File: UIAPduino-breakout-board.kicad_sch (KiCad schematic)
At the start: 5 parts, among them J1 Conn_01x20_Pin, J2 Conn_01x20_Socket

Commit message: FP 割り当て
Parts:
- J1: footprint (none) -> Connector_PinHeader_2.54mm:PinHeader_1x20_P2.54mm_Vertical
- J2: footprint (none) -> Connector_PinSocket_2.54mm:PinSocket_1x20_P2.54mm_Vertical
- JP1: footprint (none) -> Jumper:SolderJumper-2_P1.3mm_Open_TrianglePad1.0x1.5mm
- U1: footprint (none) -> akizuki:FT234X
- U2: footprint (none) -> UIAP-Devices:UIAPDUINO-PRO-MICRO-CH32V003-V1DOT4
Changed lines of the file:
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@@
 			)
 		)
-		(property "Footprint" ""
+		(property "Footprint" "Jumper:SolderJumper-2_P1.3mm_Open_TrianglePad1.0x1.5mm"
 			(at 152.4 52.07 0)
 			(effects
@@
 			)
 		)
-		(property "Footprint" ""
+		(property "Footprint" "Connector_PinHeader_2.54mm:PinHeader_1x20_P2.54mm_Vertical"
 			(at 210.82 45.72 0)
 			(effects
@@
 			)
 		)
-		(property "Footprint" ""
+		(property "Footprint" "Connector_PinSocket_2.54mm:PinSocket_1x20_P2.54mm_Vertical"
 			(at 210.82 132.08 0)
 			(effects
@@
 			)
 		)
-		(property "Footprint" ""
+		(property "Footprint" "akizuki:FT234X"
 			(at 111.76 38.1 0)
 			(effects
@@
 			)
 		)
-		(property "Footprint" ""
+		(property "Footprint" "UIAP-Devices:UIAPDUINO-PRO-MICRO-CH32V003-V1DOT4"
 			(at 152.4 58.42 0)
 			(effects

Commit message: 回路修正
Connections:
- net GND: no longer J1.7 (Pin_7), J2.7 (Pin_7)
- net at J1.8 (Pin_8), J2.8 (Pin_8): now also U2.18 (0/A1); no longer U2.22 (~{RESET})
- net at J1.9 (Pin_9), J2.9 (Pin_9), U2.17 (1/A0): no longer U2.18 (0/A1)
- new net: J1.7 (Pin_7), J2.7 (Pin_7), U2.22 (~{RESET})
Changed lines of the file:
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@@
 	(paper "A4")
 	(junction
-		(at 208.28 76.2)
-		(diameter 0)
-		(color 0 0 0 0)
-	)
-	(junction
 		(at 208.28 78.74)
 		(diameter 0)
@@
 	)
 	(junction
-		(at 205.74 66.04)
-		(diameter 0)
-		(color 0 0 0 0)
-	)
-	(junction
 		(at 223.52 81.28)
 		(diameter 0)
@@
 	)
 	(junction
+		(at 205.74 76.2)
+		(diameter 0)
+		(color 0 0 0 0)
+	)
+	(junction
 		(at 220.98 73.66)
 		(diameter 0)
@@
 	)
 	(junction
-		(at 203.2 58.42)
+		(at 203.2 66.04)
 		(diameter 0)
 		(color 0 0 0 0)
@@
 	(wire
 		(pts
-			(xy 208.28 78.74) (xy 208.28 76.2)
-		)
-		(stroke
-			(width 0)
-			(type default)
-		)
-	)
-	(wire
-		(pts
 			(xy 220.98 50.8) (xy 220.98 73.66)
 		)
@@
 	(wire
 		(pts
+			(xy 200.66 58.42) (xy 243.84 58.42)
+		)
+		(stroke
+			(width 0)
+			(type default)
+		)
+	)
+	(wire
+		(pts
 			(xy 132.08 76.2) (xy 134.62 76.2)
 		)
@@
 	(wire
 		(pts
+			(xy 203.2 66.04) (xy 203.2 127)
+		)
+		(stroke
+			(width 0)
+			(type default)
+		)
+	)
+	(wire
+		(pts
 			(xy 233.68 119.38) (xy 233.68 50.8)
 		)
@@
 	(wire
 		(pts
-			(xy 205.74 127) (xy 205.74 66.04)
+			(xy 205.74 50.8) (xy 205.74 76.2)
 		)
 		(stroke
@@
 	(wire
 		(pts
-			(xy 200.66 58.42) (xy 203.2 58.42)
-		)
-		(stroke
-			(width 0)
-			(type default)
-		)
-	)
-	(wire
-		(pts
 			(xy 170.18 60.96) (xy 172.72 60.96)
 		)
@@
 	(wire
 		(pts
-			(xy 208.28 76.2) (xy 208.28 50.8)
+			(xy 208.28 50.8) (xy 208.28 78.74)
 		)
 		(stroke
@@
 	(wire
 		(pts
-			(xy 203.2 58.42) (xy 203.2 127)
+			(xy 203.2 50.8) (xy 203.2 66.04)
 		)
 		(stroke
@@
 	(wire
 		(pts
-			(xy 203.2 50.8) (xy 203.2 58.42)
-		)
-		(stroke
-			(width 0)
-			(type default)
-		)
-	)
-	(wire
-		(pts
 			(xy 200.66 58.42) (xy 200.66 127)
 		)
@@
 	(wire
 		(pts
-			(xy 170.18 76.2) (xy 208.28 76.2)
+			(xy 170.18 76.2) (xy 205.74 76.2)
 		)
 		(stroke
@@
 	(wire
 		(pts
-			(xy 205.74 66.04) (xy 205.74 50.8)
-		)
-		(stroke
-			(width 0)
-			(type default)
-		)
-	)
-	(wire
-		(pts
 			(xy 172.72 52.07) (xy 172.72 60.96)
 		)
@@
 	(wire
 		(pts
+			(xy 205.74 76.2) (xy 205.74 127)
+		)
+		(stroke
+			(width 0)
+			(type default)
+		)
+	)
+	(wire
+		(pts
 			(xy 195.58 55.88) (xy 195.58 127)
 		)
@@
 	(wire
 		(pts
-			(xy 203.2 58.42) (xy 243.84 58.42)
-		)
-		(stroke
-			(width 0)
-			(type default)
-		)
-	)
-	(wire
-		(pts
-			(xy 170.18 66.04) (xy 205.74 66.04)
-		)
-		(stroke
+			(xy 170.18 66.04) (xy 203.2 66.04)
+		)
+		(stroke

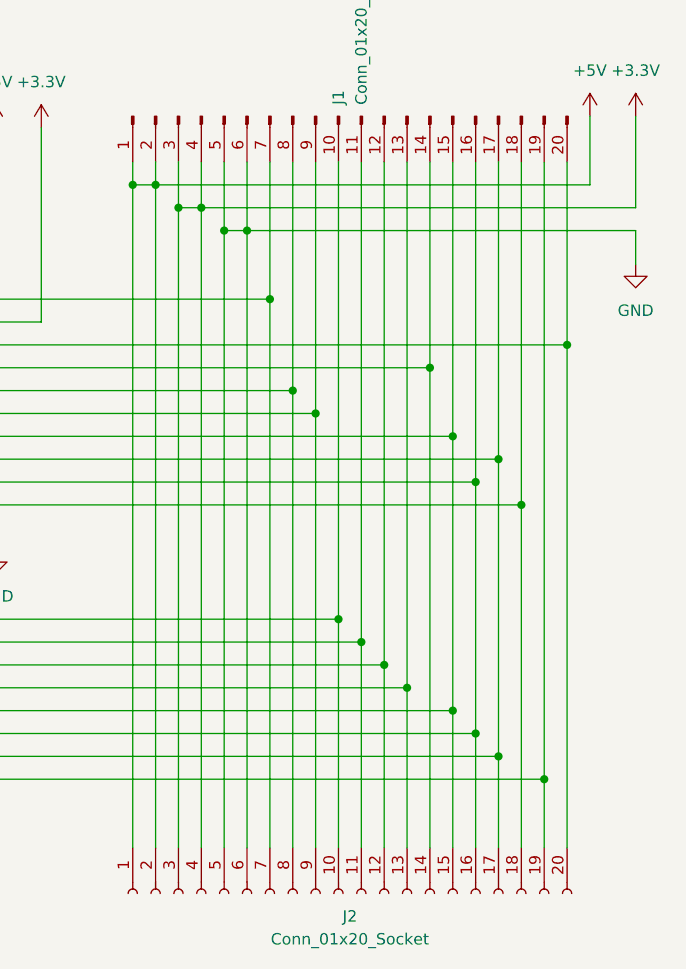
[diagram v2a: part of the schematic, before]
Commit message: 電源配置を変更
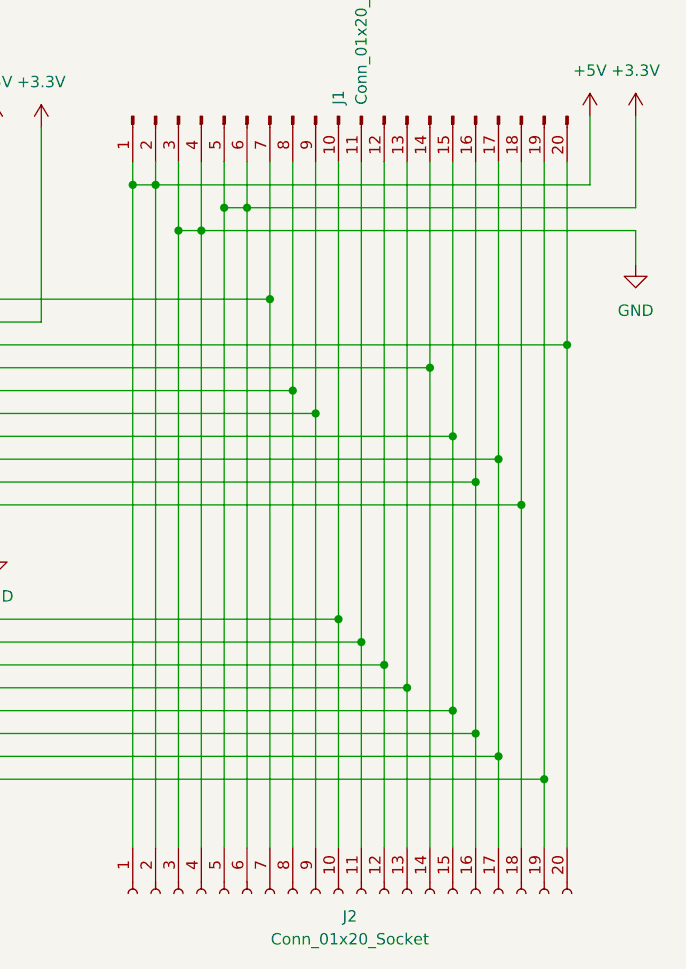
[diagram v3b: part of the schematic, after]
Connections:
- net +3.3V: now also J1.5 (Pin_5), J1.6 (Pin_6), J2.5 (Pin_5), J2.6 (Pin_6); no longer J1.3 (Pin_3), J1.4 (Pin_4), J2.3 (Pin_3), J2.4 (Pin_4)
- net GND: now also J1.3 (Pin_3), J1.4 (Pin_4), J2.3 (Pin_3), J2.4 (Pin_4); no longer J1.5 (Pin_5), J1.6 (Pin_6), J2.5 (Pin_5), J2.6 (Pin_6)
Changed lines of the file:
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@@
 	(paper "A4")
 	(junction
+		(at 195.58 58.42)
+		(diameter 0)
+		(color 0 0 0 0)
+	)
+	(junction
 		(at 208.28 78.74)
 		(diameter 0)
@@
 	)
 	(junction
+		(at 200.66 55.88)
+		(diameter 0)
+		(color 0 0 0 0)
+	)
+	(junction
 		(at 223.52 81.28)
 		(diameter 0)
@@
 	)
 	(junction
+		(at 193.04 58.42)
+		(diameter 0)
+		(color 0 0 0 0)
+	)
+	(junction
 		(at 210.82 101.6)
 		(diameter 0)
@@
 	)
 	(junction
-		(at 198.12 58.42)
-		(diameter 0)
-		(color 0 0 0 0)
-	)
-	(junction
 		(at 228.6 116.84)
 		(diameter 0)
@@
 	)
 	(junction
-		(at 195.58 55.88)
-		(diameter 0)
-		(color 0 0 0 0)
-	)
-	(junction
 		(at 190.5 53.34)
 		(diameter 0)
@@
 	)
 	(junction
-		(at 193.04 55.88)
-		(diameter 0)
-		(color 0 0 0 0)
-	)
-	(junction
 		(at 226.06 114.3)
 		(diameter 0)
@@
 	)
 	(junction
+		(at 198.12 55.88)
+		(diameter 0)
+		(color 0 0 0 0)
+	)
+	(junction
 		(at 205.74 76.2)
 		(diameter 0)
@@
 	)
 	(junction
-		(at 200.66 58.42)
-		(diameter 0)
-		(color 0 0 0 0)
-	)
-	(junction
 		(at 172.72 52.07)
 		(diameter 0)
@@
 	(wire
 		(pts
-			(xy 200.66 58.42) (xy 243.84 58.42)
-		)
-		(stroke
-			(width 0)
-			(type default)
-		)
-	)
-	(wire
-		(pts
 			(xy 132.08 76.2) (xy 134.62 76.2)
 		)
@@
 	(wire
 		(pts
+			(xy 195.58 58.42) (xy 195.58 127)
+		)
+		(stroke
+			(width 0)
+			(type default)
+		)
+	)
+	(wire
+		(pts
 			(xy 223.52 127) (xy 223.52 111.76)
 		)
@@
 	(wire
 		(pts
+			(xy 200.66 55.88) (xy 200.66 127)
+		)
+		(stroke
+			(width 0)
+			(type default)
+		)
+	)
+	(wire
+		(pts
 			(xy 233.68 119.38) (xy 233.68 50.8)
 		)
@@
 	(wire
 		(pts
-			(xy 198.12 50.8) (xy 198.12 58.42)
-		)
-		(stroke
-			(width 0)
-			(type default)
-		)
-	)
-	(wire
-		(pts
-			(xy 198.12 58.42) (xy 200.66 58.42)
+			(xy 198.12 50.8) (xy 198.12 55.88)
 		)
 		(stroke
@@
 	(wire
 		(pts
-			(xy 198.12 58.42) (xy 198.12 127)
+			(xy 198.12 55.88) (xy 198.12 127)
 		)
 		(stroke
@@
 	(wire
 		(pts
-			(xy 195.58 50.8) (xy 195.58 55.88)
+			(xy 195.58 50.8) (xy 195.58 58.42)
 		)
 		(stroke
@@
 	(wire
 		(pts
-			(xy 195.58 55.88) (xy 243.84 55.88)
-		)
-		(stroke
-			(width 0)
-			(type default)
-		)
-	)
-	(wire
-		(pts
 			(xy 170.18 73.66) (xy 220.98 73.66)
 		)
@@
 	(wire
 		(pts
-			(xy 193.04 55.88) (xy 193.04 127)
-		)
-		(stroke
-			(width 0)
-			(type default)
-		)
-	)
-	(wire
-		(pts
 			(xy 129.54 73.66) (xy 129.54 106.68)
 		)
@@
 	(wire
 		(pts
-			(xy 193.04 55.88) (xy 195.58 55.88)
-		)
-		(stroke
-			(width 0)
-			(type default)
-		)
-	)
-	(wire
-		(pts
 			(xy 128.27 109.22) (xy 218.44 109.22)
 		)
@@
 	(wire
 		(pts
+			(xy 198.12 55.88) (xy 200.66 55.88)
+		)
+		(stroke
+			(width 0)
+			(type default)
+		)
+	)
+	(wire
+		(pts
 			(xy 177.8 46.99) (xy 177.8 68.58)
 		)
@@
 	(wire
 		(pts
-			(xy 193.04 50.8) (xy 193.04 55.88)
-		)
-		(stroke
-			(width 0)
-			(type default)
-		)
-	)
-	(wire
-		(pts
-			(xy 200.66 50.8) (xy 200.66 58.42)
+			(xy 193.04 50.8) (xy 193.04 58.42)
+		)
+		(stroke
+			(width 0)
+			(type default)
+		)
+	)
+	(wire
+		(pts
+			(xy 200.66 50.8) (xy 200.66 55.88)
 		)
 		(stroke
@@
 	(wire
 		(pts
-			(xy 200.66 58.42) (xy 200.66 127)
+			(xy 193.04 58.42) (xy 193.04 127)
 		)
 		(stroke
@@
 	(wire
 		(pts
+			(xy 195.58 58.42) (xy 243.84 58.42)
+		)
+		(stroke
+			(width 0)
+			(type default)
+		)
+	)
+	(wire
+		(pts
 			(xy 119.38 68.58) (xy 119.38 66.04)
 		)
@@
 	(wire
 		(pts
-			(xy 195.58 55.88) (xy 195.58 127)
+			(xy 200.66 55.88) (xy 243.84 55.88)
 		)
 		(stroke
@@
 		)
 		(stroke
+			(width 0)
+			(type default)
+		)
+	)
+	(wire
+		(pts
+			(xy 193.04 58.42) (xy 195.58 58.42)
+		)
+		(stroke

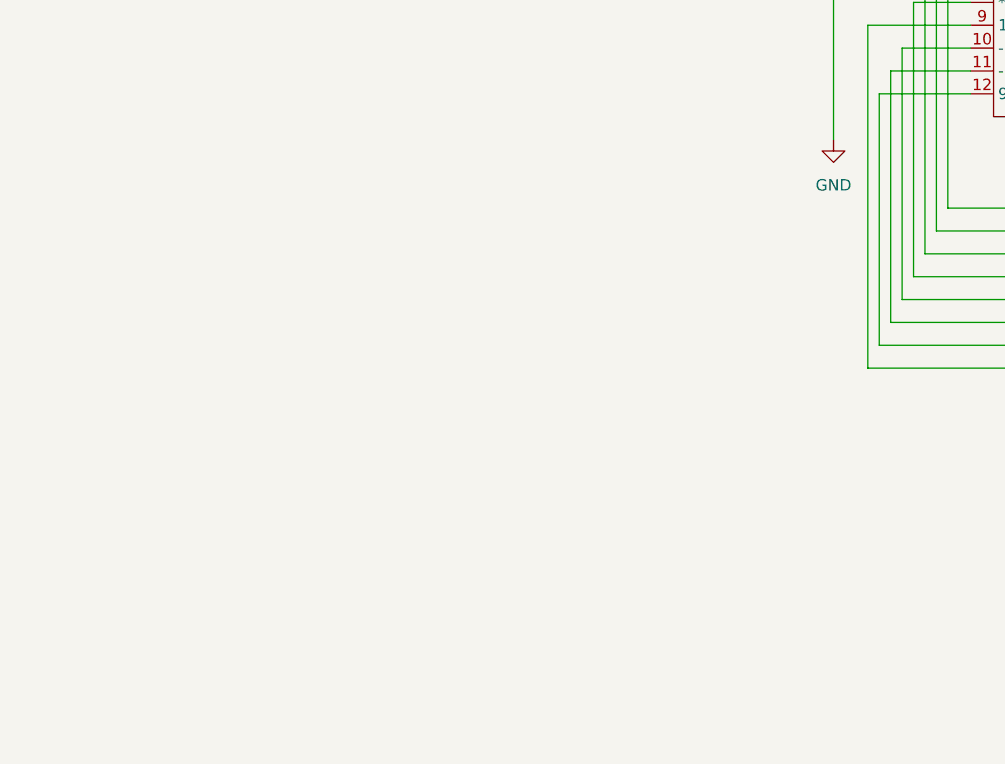
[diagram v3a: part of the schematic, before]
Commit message: 電源入力回路追加
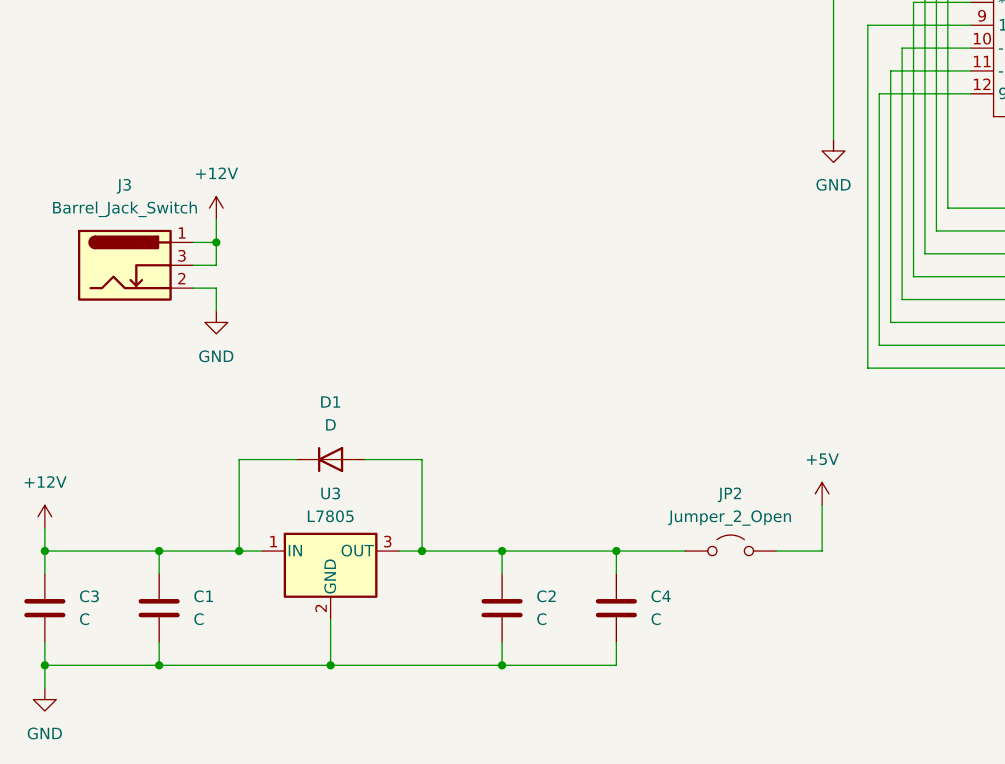
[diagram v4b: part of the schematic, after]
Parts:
- added C1, C2, C3, C4: C, symbol Device:C
- added D1: D, symbol Device:D
- added J3: Barrel_Jack_Switch, symbol Connector:Barrel_Jack_Switch
- added JP2: Jumper_2_Open, Jumper:SolderJumper-2_P1.3mm_Open_TrianglePad1.0x1.5mm, symbol Jumper:Jumper_2_Open
- added U3: L7805, symbol Regulator_Linear:L7805
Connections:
- net +5V: now also JP2.2 (B)
- net GND: now also C1.2, C2.2, C3.2, C4.2, J3.2, U3.2 (GND)
- new net: C2.1, C4.1, D1.2 (A), JP2.1 (A), U3.3 (OUT)
- new net +12V: C1.1, C3.1, D1.1 (K), J3.1, J3.3, U3.1 (IN)

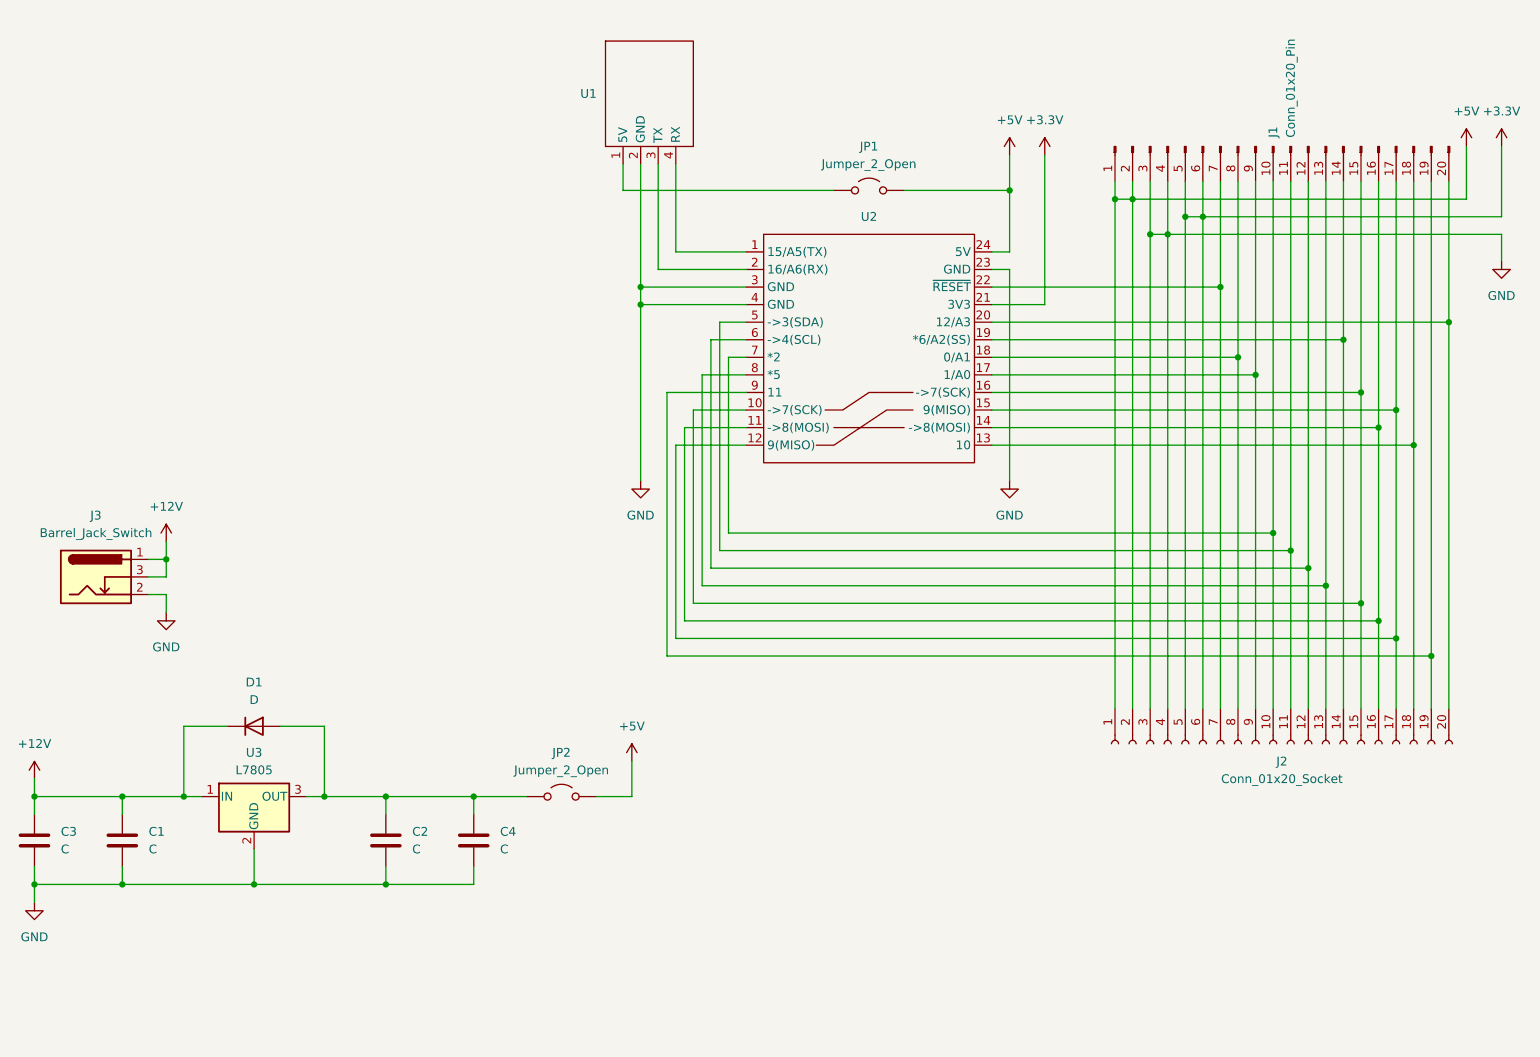
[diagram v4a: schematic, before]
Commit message: FP 割り当て
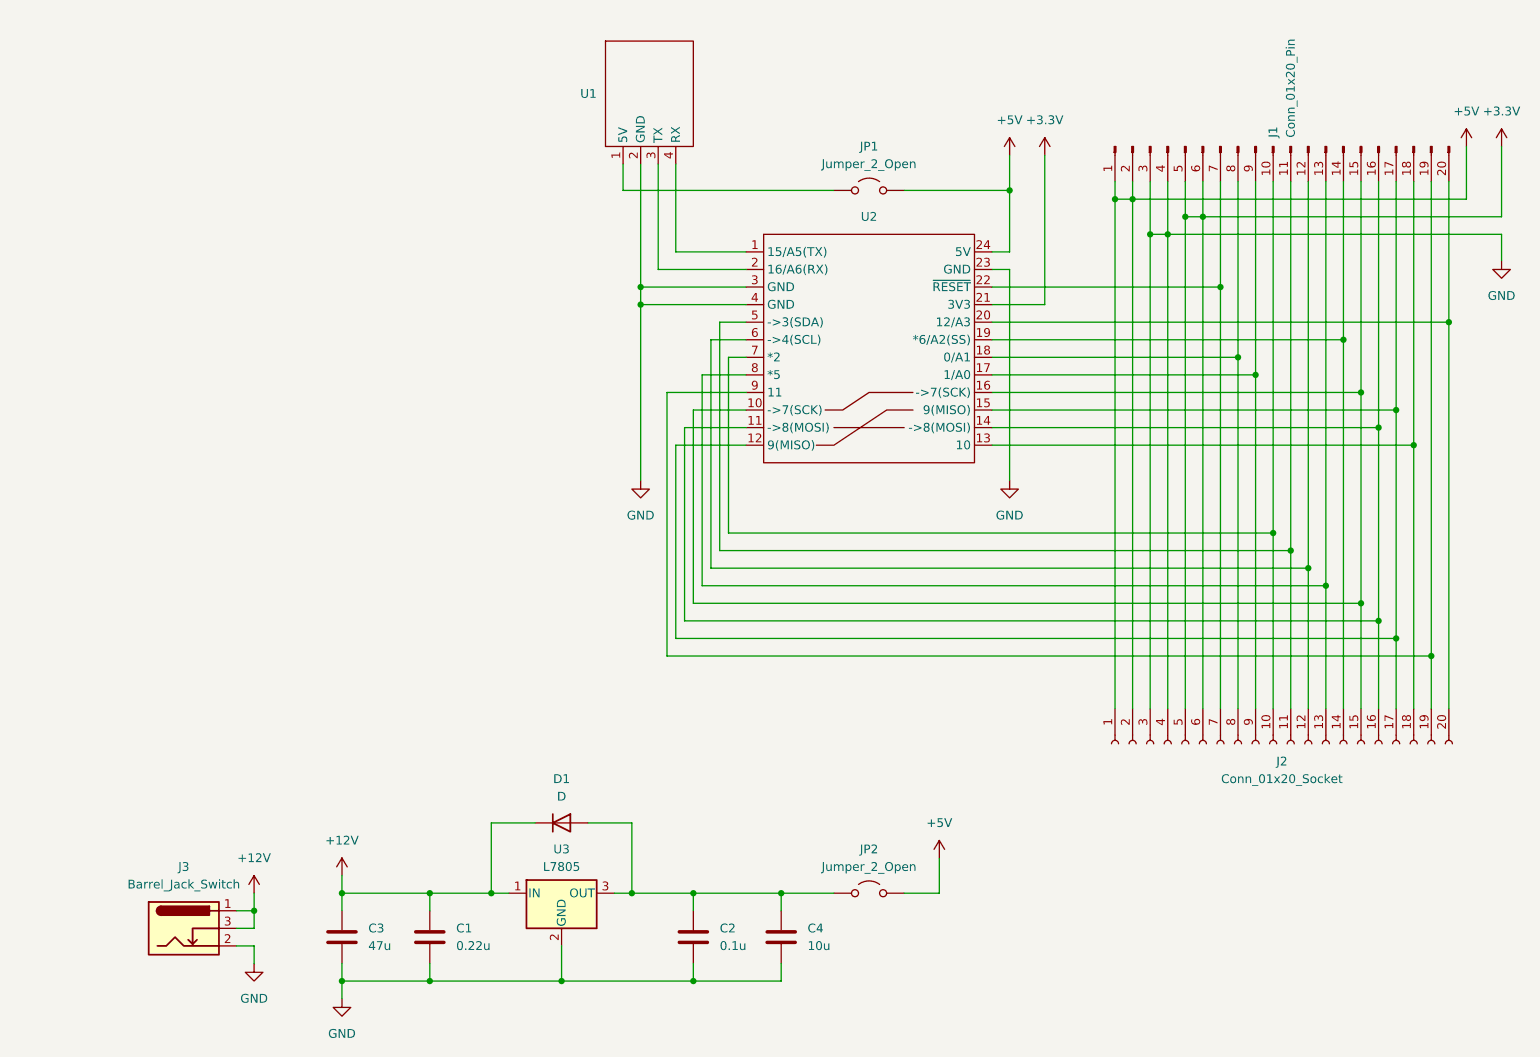
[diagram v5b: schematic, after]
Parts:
- C1: value C -> 0.22u; footprint (none) -> Capacitor_THT:C_Disc_D5.0mm_W2.5mm_P5.00mm
- C2: value C -> 0.1u; footprint (none) -> Capacitor_THT:C_Disc_D5.0mm_W2.5mm_P5.00mm
- C3: value C -> 47u; footprint (none) -> Capacitor_THT:CP_Radial_D5.0mm_P2.00mm
- C4: value C -> 10u; footprint (none) -> Capacitor_THT:CP_Radial_D4.0mm_P1.50mm
- D1: footprint (none) -> Diode_THT:D_A-405_P7.62mm_Horizontal
- J3: footprint (none) -> Connector_BarrelJack:BarrelJack_Horizontal
- U3: footprint (none) -> Package_TO_SOT_THT:TO-220F-3_Horizontal_TabDown
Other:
- moved on the sheet: C1, C2, C3, C4, D1, J3, JP2, U3

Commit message: JP の向きを反転
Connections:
- net +5V: now also JP1.1 (A), JP2.1 (A); no longer JP1.2 (B), JP2.2 (B)
- net at U1.1 (5V): now also JP1.2 (B); no longer JP1.1 (A)
- net at C2.1, C4.1, D1.2 (A)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: now also JP2.2 (B); no longer JP2.1 (A)
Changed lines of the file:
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@@
 		(lib_id "Jumper:Jumper_2_Open")
 		(at 152.4 52.07 0)
+		(mirror y)
 		(unit 1)
 		(exclude_from_sim yes)
@@
 		(on_board yes)
 		(dnp no)
-		(fields_autoplaced yes)
 		(property "Reference" "JP1"
 			(at 152.4 45.72 0)
@@
 		(lib_id "Jumper:Jumper_2_Open")
 		(at 152.4 153.67 0)
+		(mirror y)
 		(unit 1)
 		(exclude_from_sim yes)
@@
 		(on_board yes)
 		(dnp no)
-		(fields_autoplaced yes)
 		(property "Reference" "JP2"
 			(at 152.4 147.32 0)

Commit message: 7805 の FP 変更
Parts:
- U3: footprint Package_TO_SOT_THT:TO-220F-3_Horizontal_TabDown -> Package_TO_SOT_THT:TO-220F-3_Vertical
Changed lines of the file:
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@@
 			)
 		)
-		(property "Footprint" "Package_TO_SOT_THT:TO-220F-3_Horizontal_TabDown"
+		(property "Footprint" "Package_TO_SOT_THT:TO-220F-3_Vertical"
 			(at 108.585 157.48 0)
 			(effects
